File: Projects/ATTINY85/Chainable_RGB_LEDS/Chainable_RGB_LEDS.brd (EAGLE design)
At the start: 45.7 x 57.2 mm, 13 parts, among them IC1 ATTINY85

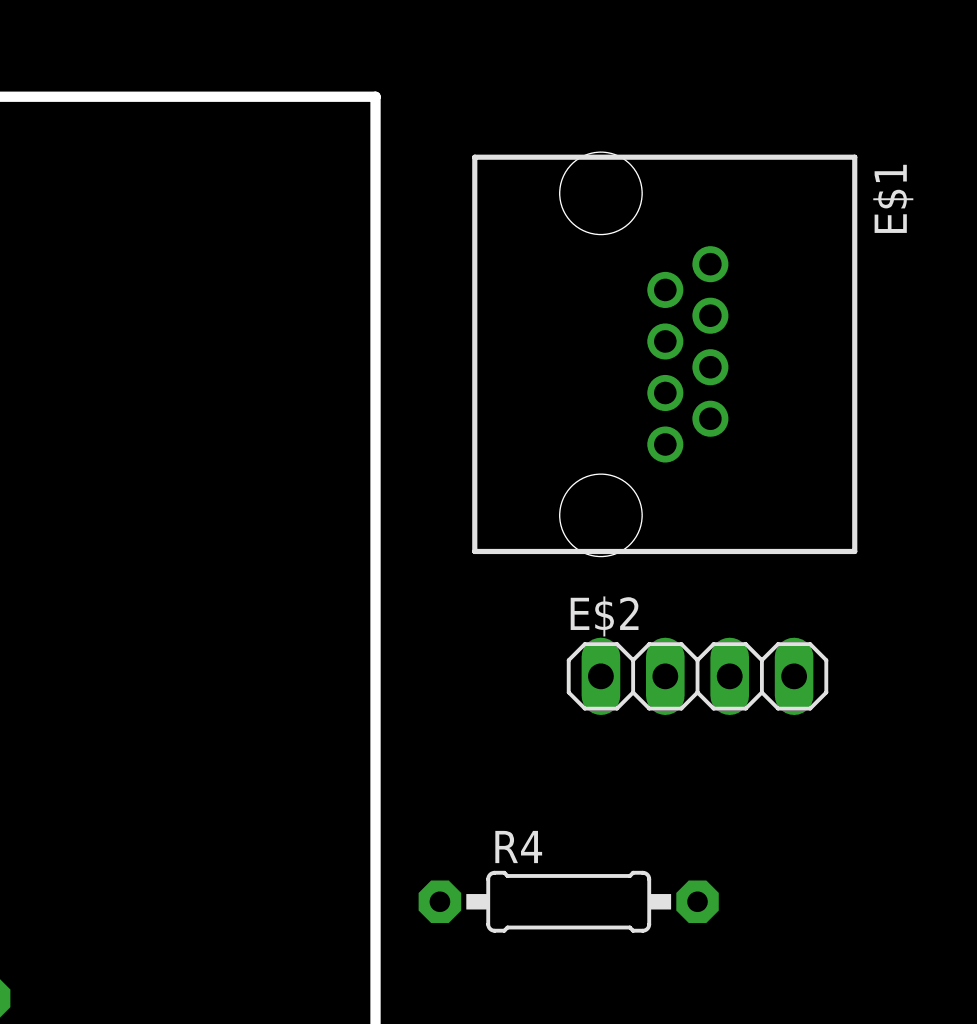
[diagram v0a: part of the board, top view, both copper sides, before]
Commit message: Add SparkFun Eagle Libraries
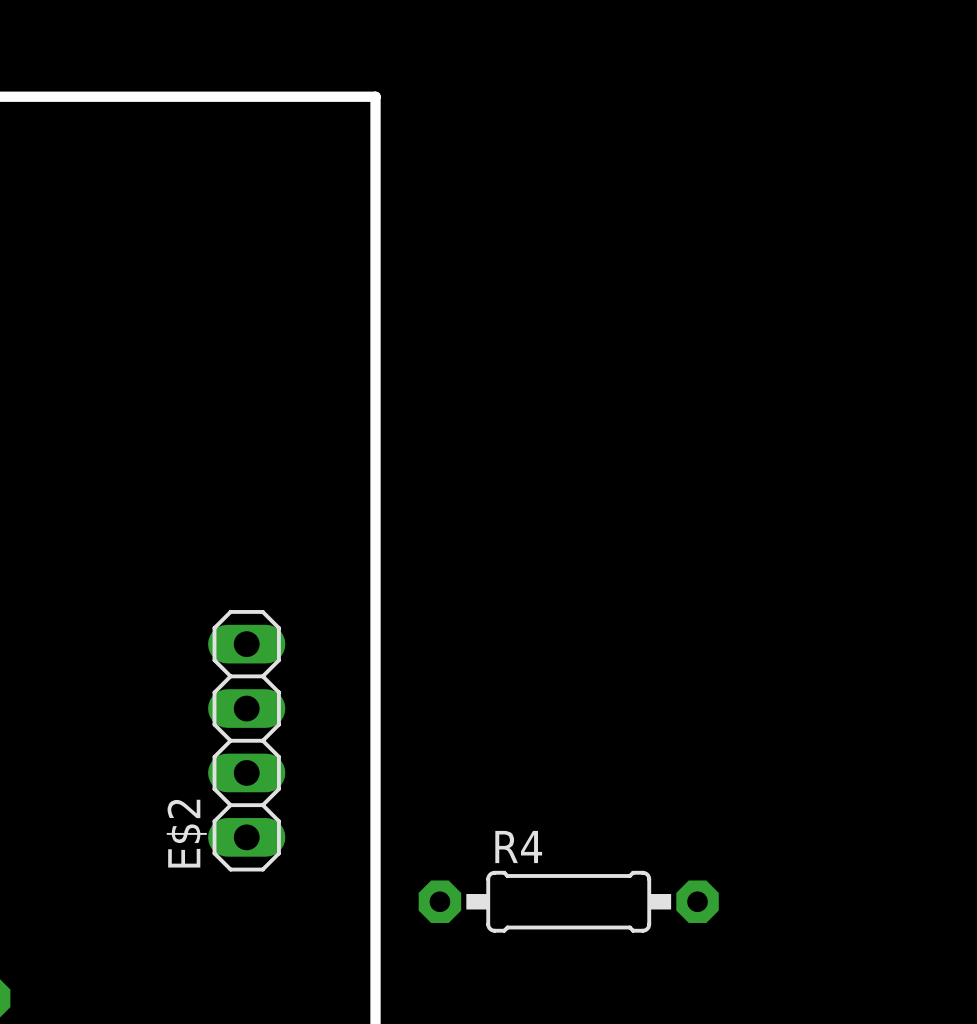
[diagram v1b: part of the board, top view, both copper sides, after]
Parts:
- removed E$1: (no value), con-molex:0446200001
- moved E$2 18.0 mm to (48.3, 40.6), turned to 90 degrees
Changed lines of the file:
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@@
 </autorouter>
 <elements>
-<element name="E$1" library="con-molex" package="0446200001" value="" x="62.23" y="55.88" rot="R270"/>
-<element name="E$2" library="pinhead" package="1X04" value="" x="66.04" y="43.18"/>
+<element name="E$2" library="pinhead" package="1X04" value="" x="48.26" y="40.64" rot="R90"/>
 <element name="IC1" library="SparkFun-DigitalIC" package="DIP08" value="ATTINY85" x="30.48" y="40.64" rot="R180"/>
 <element name="LM7805" library="SparkFun-PowerIC" package="78XXL" value="" x="15.24" y="20.32"/>

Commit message: v1.0 Board Completed
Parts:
- removed E$2: (no value), pinhead:1X04
- removed E$5, E$6: (no value), con-molex:7395-02
- removed E$9: (no value), pinhead:1X03
- added CAP1: 0.33uF, SparkFun-Capacitors-Updated:CAP-PTH-SMALL-KIT
- added CAP2: 0.1uF, SparkFun-Capacitors-Updated:CAP-PTH-SMALL-KIT
- added DRILEGEND: (no value), drilegend:DRILEGEND
- added PWR, SW: (no value), con-molex:7395-02
- added RGBLED: (no value), con-molex:7395-04
- LM7805: value (none) -> VREG; device SparkFun-PowerIC:78XXL -> SparkFun-PowerIC:TO-220-ALT
- R1, R2, R3: value 330 -> 330R
- moved R4 50.7 mm to (14.0, 53.3), turned to 90 degrees
- moved VR 11.7 mm to (36.8, 58.4)
- moved R1 6.48 mm to (25.4, 49.5), turned to 90 degrees
- moved BTN 5.68 mm to (20.3, 58.4)
- moved IC1 5.39 mm to (26.7, 36.8)
- moved LM7805 5.24 mm to (14.0, 25.4)
- moved R3 4.58 mm to (29.2, 27.9), turned to 180 degrees
- moved R2 4.58 mm to (26.7, 24.1), turned to 180 degrees
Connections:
- removed net S$5: IC1.5, R2.1
- new net S$10: R2.1, RGBLED.4
- new net S$12: BTN.2, IC1.4, LM7805.GND, PWR.2, RGBLED.2, VR.3
- new net S$13: IC1.8, LM7805.IN, R4.1, VR.1
- new net S$14: IC1.3, R1.1
- new net S$15: BTN.1, IC1.2, R4.2
- new net S$7: R3.1, RGBLED.3
- new net S$8: IC1.6, R3.2
- new net S$9: IC1.5, R2.2
- net S$1: now also LM7805.OUT, SW.1; no longer IC1.6, R3.1
- net S$2: now also PWR.1, SW.2; no longer E$5.2, LM7805.GND
- net S$3: now also R1.2, RGBLED.1; no longer E$6.1, LM7805.OUT
- net S$6: now also IC1.7, VR.2; no longer E$5.1, E$6.2
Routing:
- net S$12: track 0.00 -> 141.9 mm
- net S$13: track 0.00 -> 79.1 mm
- net S$15: track 0.00 -> 35.3 mm
- net S$6: track 3.81 -> 36.4 mm
- net S$2: track 35.6 -> 3.81 mm
- net S$1: track 6.88 -> 30.8 mm
- net S$10: track 0.00 -> 17.1 mm
- net S$7: track 0.00 -> 14.1 mm
- net S$5: track 10.7 -> 0.00 mm
- net S$9: track 0.00 -> 9.42 mm
- net S$8: track 0.00 -> 5.61 mm
- net S$3: track 35.3 -> 40.2 mm
- net S$14: track 0.00 -> 3.81 mm
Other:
- board size 45.7 x 57.2 mm -> 39.4 x 50.8 mm
- board text added: "01-16"
- board text added: "01-20"
- board text added: "David Thornton"
- board text added: "LAYER-STACK"
- board text added: "RGB Moodlamp"
- board text added: "v1.0"
